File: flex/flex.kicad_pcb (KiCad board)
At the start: 2 copper layers, 40.1 x 42.3 mm, 14 parts, among them J2 Conn_01x01_Socket, J7 Conn_01x07_Socket, SW5 SW_Push, SW6 SW_Push, SW7 SW_Push, SW8 SW_Push

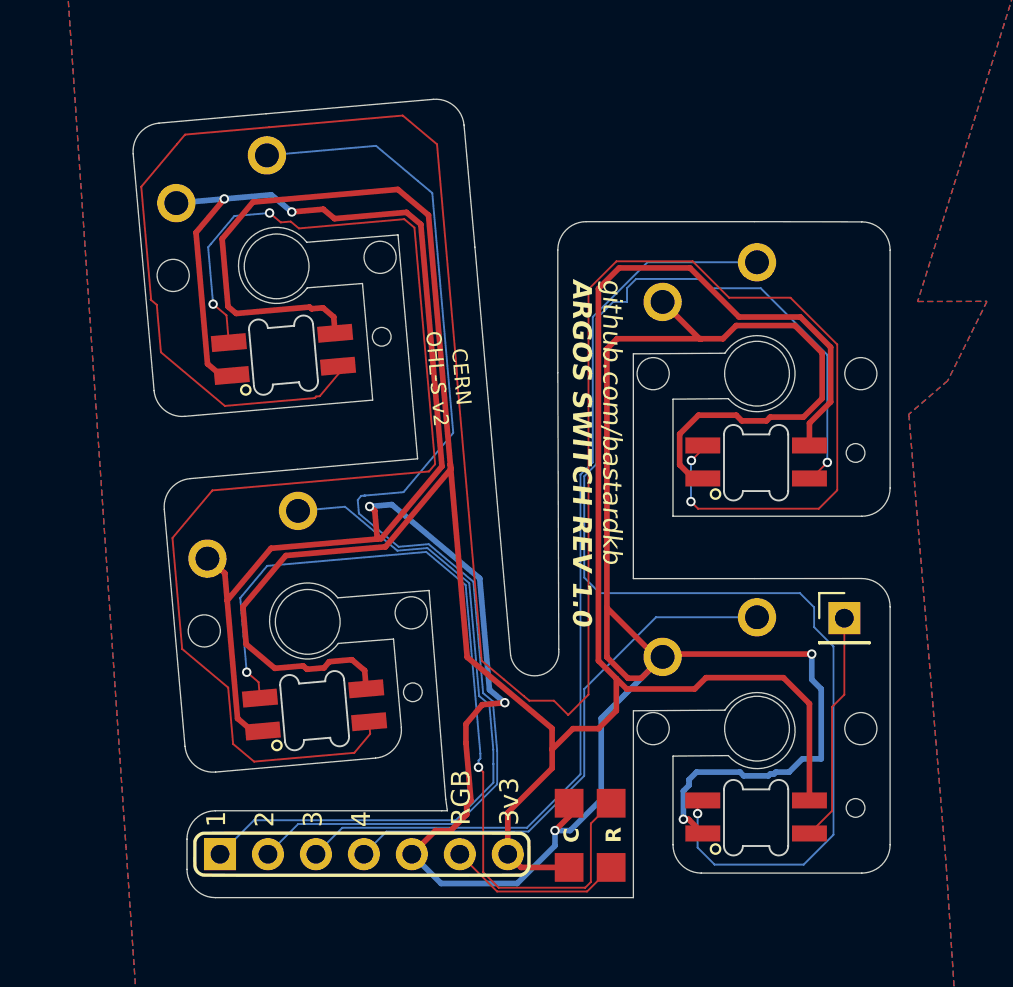
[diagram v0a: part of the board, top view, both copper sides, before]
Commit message: switch numbering
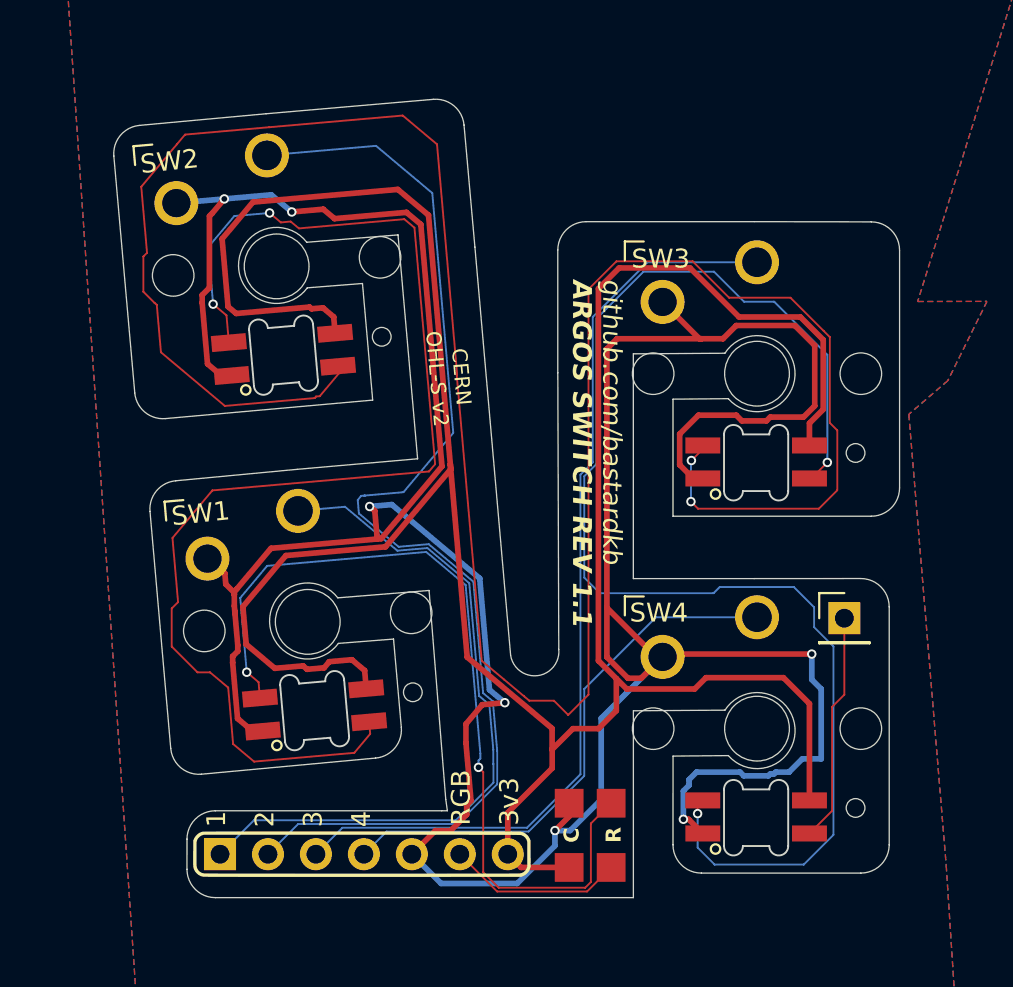
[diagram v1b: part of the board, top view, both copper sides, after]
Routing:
- net Net-(D13-DOUT): track 66.3 -> 67.0 mm
- net Gnd: track 191.9 -> 191.3 mm
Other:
- board size 40.1 x 42.3 mm -> 41.6 x 42.3 mm
- board text added: "ARGOS SWITCH REV 1.1"
- board text removed: "ARGOS SWITCH REV 1.0"
